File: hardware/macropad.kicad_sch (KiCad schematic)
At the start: 26 parts, among them J2 Conn_01x06, J3 I2C Screen, J4 SPI Screen, SW1 SW_Push, SW2 SW_Push, SW3 SW_Push, SW4 SW_Push, SW5 SW_Push, SW6 SW_Push, SW7 SW_Push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

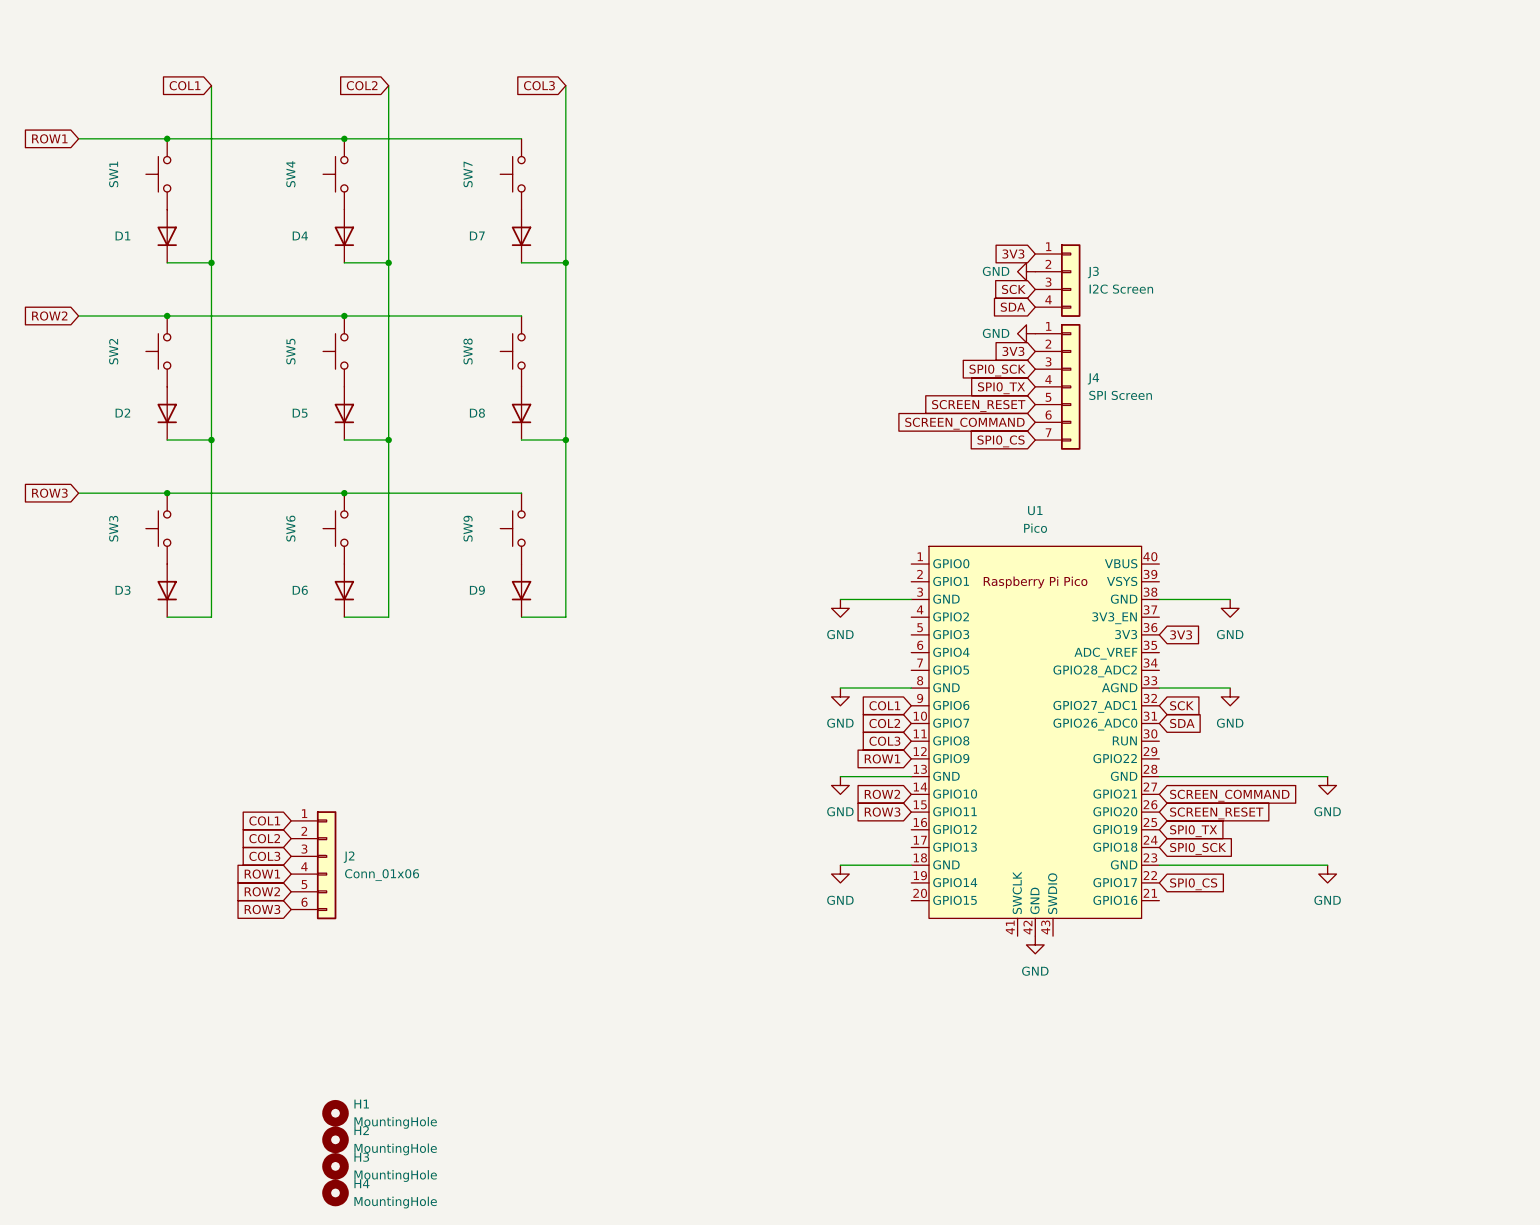
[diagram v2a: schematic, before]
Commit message: :truck: Test different layout with pi pico in the back
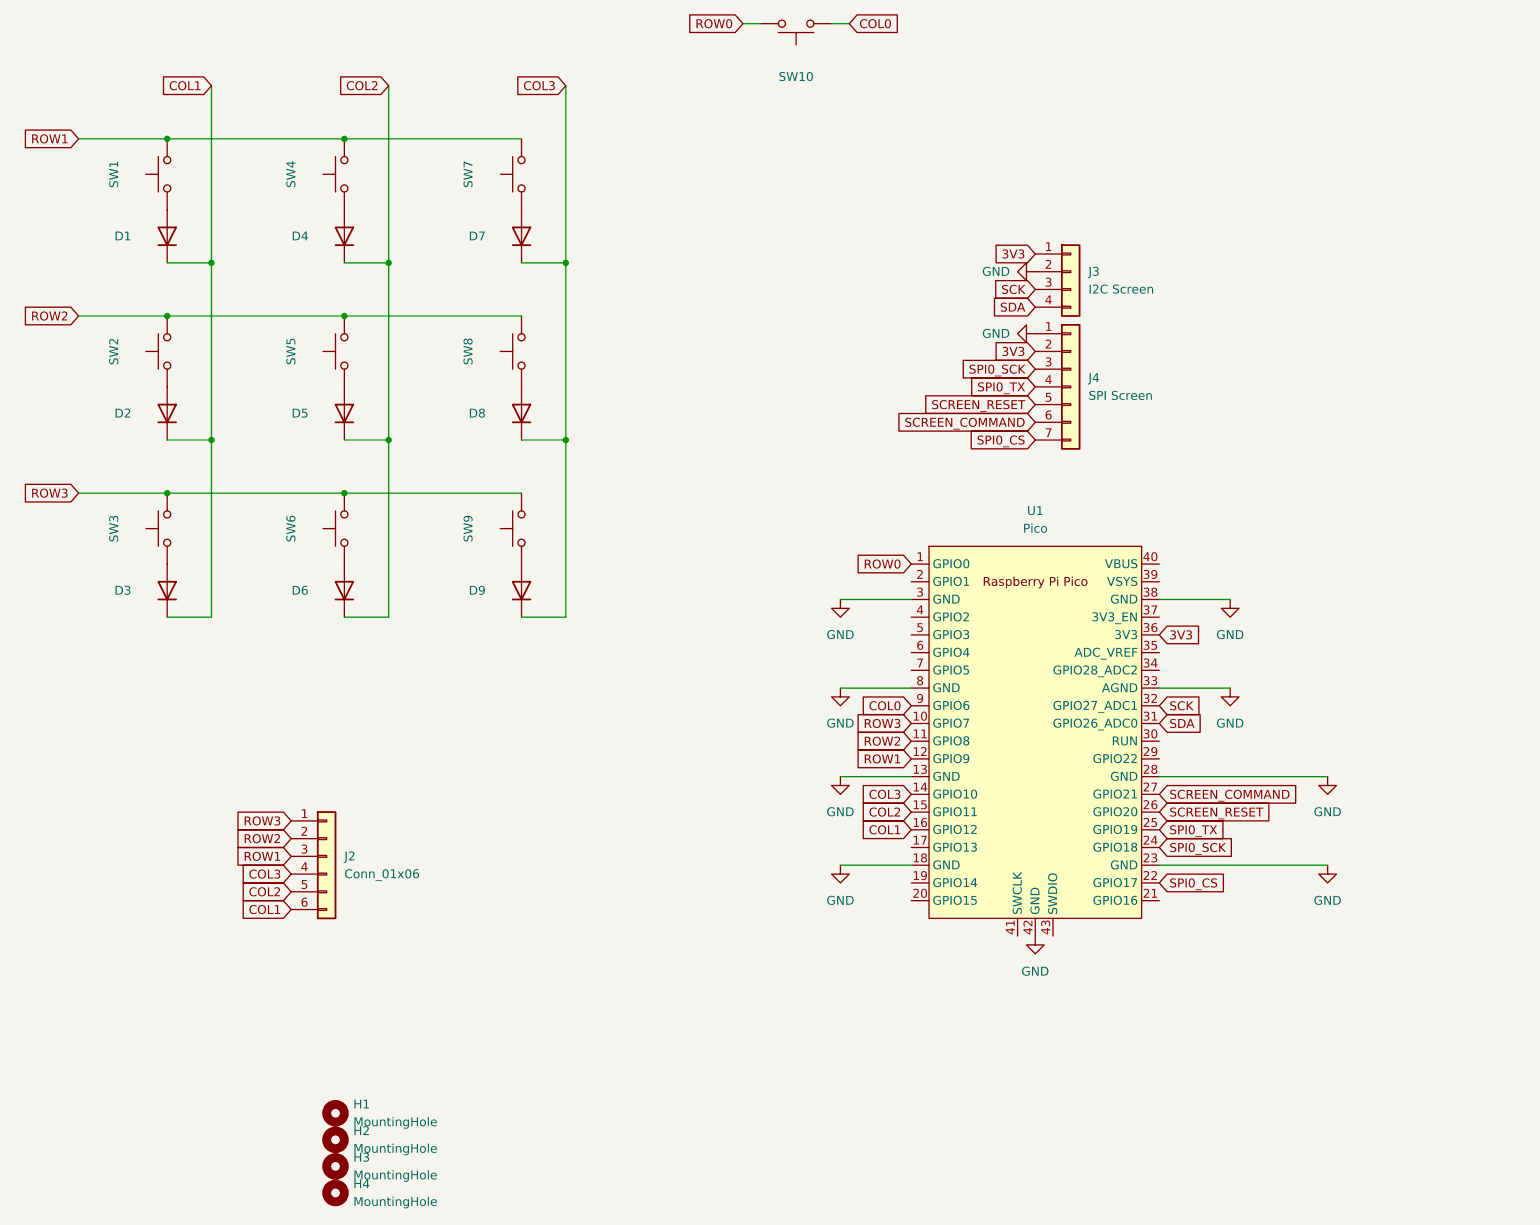
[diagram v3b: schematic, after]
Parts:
- added SW10: SW_Push, Switch_Keyboard_Hotswap_Kailh:SW_Hotswap_Kailh_MX, symbol Switch:SW_Push
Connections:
- net COL1: now also J2.6 (Pin_6), U1.16 (GPIO12); no longer J2.1 (Pin_1), U1.9 (GPIO6)
- net COL2: now also J2.5 (Pin_5), U1.15 (GPIO11); no longer J2.2 (Pin_2), U1.10 (GPIO7)
- net COL3: now also J2.4 (Pin_4), U1.14 (GPIO10); no longer J2.3 (Pin_3), U1.11 (GPIO8)
- net ROW1: now also J2.3 (Pin_3); no longer J2.4 (Pin_4)
- net ROW2: now also J2.2 (Pin_2), U1.11 (GPIO8); no longer J2.5 (Pin_5), U1.14 (GPIO10)
- net ROW3: now also J2.1 (Pin_1), U1.10 (GPIO7); no longer J2.6 (Pin_6), U1.15 (GPIO11)
- net ROW0: now reaches U1.1 (GPIO0)
- net ROW0: now also SW10.1
- new net COL0: SW10.2, U1.9 (GPIO6)
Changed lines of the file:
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@@
+    (stroke (width 0) (type default) (color 0 0 0 0))
+  )
+  (wire (pts (xy 177.8 22.86) (xy 175.26 22.86))
     (stroke (width 0) (type default) (color 0 0 0 0))
   )
@@
   )
   (wire (pts (xy 80.01 90.17) (xy 105.41 90.17))
+    (stroke (width 0) (type default) (color 0 0 0 0))
+  )
+  (wire (pts (xy 162.56 22.86) (xy 165.1 22.86))
     (stroke (width 0) (type default) (color 0 0 0 0))
   )
@@
     )
   )
+  (global_label "ROW0" (shape input) (at 186.69 100.33 180) (fields_autoplaced)
+    (effects (font (size 1.27 1.27)) (justify right))
+    (property "Intersheet References" "${INTERSHEET_REFS}" (id 0) (at 179.0155 100.2506 0)
+      (effects (font (size 1.27 1.27)) (justify right) hide)
+    )
+  )
   (global_label "SCK" (shape input) (at 204.47 60.96 180) (fields_autoplaced)
     (effects (font (size 1.27 1.27)) (justify right))
@@
     )
   )
-  (global_label "COL2" (shape input) (at 97.79 139.7 180) (fields_autoplaced)
-    (effects (font (size 1.27 1.27)) (justify right))
-    (property "Intersheet References" "${INTERSHEET_REFS}" (id 0) (at 90.5388 139.6206 0)
+  (global_label "COL2" (shape input) (at 97.79 147.32 180) (fields_autoplaced)
+    (effects (font (size 1.27 1.27)) (justify right))
+    (property "Intersheet References" "${INTERSHEET_REFS}" (id 0) (at 90.5388 147.3994 0)
       (effects (font (size 1.27 1.27)) (justify right) hide)
     )
@@
     )
   )
-  (global_label "COL3" (shape input) (at 186.69 125.73 180) (fields_autoplaced)
-    (effects (font (size 1.27 1.27)) (justify right))
-    (property "Intersheet References" "${INTERSHEET_REFS}" (id 0) (at 179.4388 125.6506 0)
-      (effects (font (size 1.27 1.27)) (justify right) hide)
-    )
-  )
-  (global_label "ROW3" (shape input) (at 186.69 135.89 180) (fields_autoplaced)
-    (effects (font (size 1.27 1.27)) (justify right))
-    (property "Intersheet References" "${INTERSHEET_REFS}" (id 0) (at 179.0155 135.8106 0)
+  (global_label "COL3" (shape input) (at 186.69 133.35 180) (fields_autoplaced)
+    (effects (font (size 1.27 1.27)) (justify right))
+    (property "Intersheet References" "${INTERSHEET_REFS}" (id 0) (at 179.4388 133.2706 0)
+      (effects (font (size 1.27 1.27)) (justify right) hide)
+    )
+  )
+  (global_label "ROW3" (shape input) (at 186.69 123.19 180) (fields_autoplaced)
+    (effects (font (size 1.27 1.27)) (justify right))
+    (property "Intersheet References" "${INTERSHEET_REFS}" (id 0) (at 179.0155 123.1106 0)
       (effects (font (size 1.27 1.27)) (justify right) hide)
     )
@@
     )
   )
-  (global_label "COL3" (shape input) (at 97.79 142.24 180) (fields_autoplaced)
-    (effects (font (size 1.27 1.27)) (justify right))
-    (property "Intersheet References" "${INTERSHEET_REFS}" (id 0) (at 90.5388 142.1606 0)
-      (effects (font (size 1.27 1.27)) (justify right) hide)
-    )
-  )
-  (global_label "COL1" (shape input) (at 97.79 137.16 180) (fields_autoplaced)
-    (effects (font (size 1.27 1.27)) (justify right))
-    (property "Intersheet References" "${INTERSHEET_REFS}" (id 0) (at 90.5388 137.0806 0)
-      (effects (font (size 1.27 1.27)) (justify right) hide)
-    )
-  )
-  (global_label "COL1" (shape input) (at 186.69 120.65 180) (fields_autoplaced)
-    (effects (font (size 1.27 1.27)) (justify right))
-    (property "Intersheet References" "${INTERSHEET_REFS}" (id 0) (at 179.4388 120.5706 0)
+  (global_label "COL3" (shape input) (at 97.79 144.78 180) (fields_autoplaced)
+    (effects (font (size 1.27 1.27)) (justify right))
+    (property "Intersheet References" "${INTERSHEET_REFS}" (id 0) (at 90.5388 144.8594 0)
+      (effects (font (size 1.27 1.27)) (justify right) hide)
+    )
+  )
+  (global_label "COL1" (shape input) (at 97.79 149.86 180) (fields_autoplaced)
+    (effects (font (size 1.27 1.27)) (justify right))
+    (property "Intersheet References" "${INTERSHEET_REFS}" (id 0) (at 90.5388 149.9394 0)
+      (effects (font (size 1.27 1.27)) (justify right) hide)
+    )
+  )
+  (global_label "COL1" (shape input) (at 186.69 138.43 180) (fields_autoplaced)
+    (effects (font (size 1.27 1.27)) (justify right))
+    (property "Intersheet References" "${INTERSHEET_REFS}" (id 0) (at 179.4388 138.3506 0)
       (effects (font (size 1.27 1.27)) (justify right) hide)
     )
@@
     )
   )
+  (global_label "COL0" (shape input) (at 177.8 22.86 0) (fields_autoplaced)
+    (effects (font (size 1.27 1.27)) (justify left))
+    (property "Intersheet References" "${INTERSHEET_REFS}" (id 0) (at 185.0512 22.9394 0)
+      (effects (font (size 1.27 1.27)) (justify left) hide)
+    )
+  )
   (global_label "SDA" (shape input) (at 222.25 123.19 0) (fields_autoplaced)
     (effects (font (size 1.27 1.27)) (justify left))
@@
     )
   )
-  (global_label "COL2" (shape input) (at 186.69 123.19 180) (fields_autoplaced)
-    (effects (font (size 1.27 1.27)) (justify right))
-    (property "Intersheet References" "${INTERSHEET_REFS}" (id 0) (at 179.4388 123.1106 0)
+  (global_label "COL2" (shape input) (at 186.69 135.89 180) (fields_autoplaced)
+    (effects (font (size 1.27 1.27)) (justify right))
+    (property "Intersheet References" "${INTERSHEET_REFS}" (id 0) (at 179.4388 135.8106 0)
       (effects (font (size 1.27 1.27)) (justify right) hide)
     )
@@
     (effects (font (size 1.27 1.27)) (justify right))
     (property "Intersheet References" "${INTERSHEET_REFS}" (id 0) (at 198.5493 69.9294 0)
+      (effects (font (size 1.27 1.27)) (justify right) hide)
+    )
+  )
+  (global_label "COL0" (shape input) (at 186.69 120.65 180) (fields_autoplaced)
+    (effects (font (size 1.27 1.27)) (justify right))
+    (property "Intersheet References" "${INTERSHEET_REFS}" (id 0) (at 179.4388 120.5706 0)
       (effects (font (size 1.27 1.27)) (justify right) hide)
     )
@@
     )
   )
-  (global_label "ROW2" (shape input) (at 97.79 147.32 180) (fields_autoplaced)
-    (effects (font (size 1.27 1.27)) (justify right))
-    (property "Intersheet References" "${INTERSHEET_REFS}" (id 0) (at 90.1155 147.2406 0)
+  (global_label "ROW2" (shape input) (at 97.79 139.7 180) (fields_autoplaced)
+    (effects (font (size 1.27 1.27)) (justify right))
+    (property "Intersheet References" "${INTERSHEET_REFS}" (id 0) (at 90.1155 139.7794 0)
       (effects (font (size 1.27 1.27)) (justify right) hide)
     )
@@
     )
   )
-  (global_label "ROW1" (shape input) (at 97.79 144.78 180) (fields_autoplaced)
-    (effects (font (size 1.27 1.27)) (justify right))
-    (property "Intersheet References" "${INTERSHEET_REFS}" (id 0) (at 90.1155 144.7006 0)
-      (effects (font (size 1.27 1.27)) (justify right) hide)
-    )
-  )
-  (global_label "ROW3" (shape input) (at 97.79 149.86 180) (fields_autoplaced)
-    (effects (font (size 1.27 1.27)) (justify right))
-    (property "Intersheet References" "${INTERSHEET_REFS}" (id 0) (at 90.1155 149.7806 0)
+  (global_label "ROW1" (shape input) (at 97.79 142.24 180) (fields_autoplaced)
+    (effects (font (size 1.27 1.27)) (justify right))
+    (property "Intersheet References" "${INTERSHEET_REFS}" (id 0) (at 90.1155 142.3194 0)
+      (effects (font (size 1.27 1.27)) (justify right) hide)
+    )
+  )
+  (global_label "ROW3" (shape input) (at 97.79 137.16 180) (fields_autoplaced)
+    (effects (font (size 1.27 1.27)) (justify right))
+    (property "Intersheet References" "${INTERSHEET_REFS}" (id 0) (at 90.1155 137.2394 0)
+      (effects (font (size 1.27 1.27)) (justify right) hide)
+    )
+  )
+  (global_label "ROW0" (shape input) (at 162.56 22.86 180) (fields_autoplaced)
+    (effects (font (size 1.27 1.27)) (justify right))
+    (property "Intersheet References" "${INTERSHEET_REFS}" (id 0) (at 154.8855 22.7806 0)
       (effects (font (size 1.27 1.27)) (justify right) hide)
     )
@@
     )
   )
-  (global_label "ROW2" (shape input) (at 186.69 133.35 180) (fields_autoplaced)
-    (effects (font (size 1.27 1.27)) (justify right))
-    (property "Intersheet References" "${INTERSHEET_REFS}" (id 0) (at 179.0155 133.2706 0)
+  (global_label "ROW2" (shape input) (at 186.69 125.73 180) (fields_autoplaced)
+    (effects (font (size 1.27 1.27)) (justify right))
+    (property "Intersheet References" "${INTERSHEET_REFS}" (id 0) (at 179.0155 125.6506 0)
       (effects (font (size 1.27 1.27)) (justify right) hide)
     )
@@
     )
     (pin "1")
+  )
+  (symbol (lib_id "Switch:SW_Push") (at 170.18 22.86 0) (mirror x) (unit 1)
+    (in_bom yes) (on_board yes)
+    (property "Reference" "SW10" (id 0) (at 170.18 30.48 0))
+    (property "Value" "SW_Push" (id 1) (at 170.18 17.78 90)
+      (effects (font (size 1.27 1.27)) hide)
+    )
+    (property "Footprint" "Switch_Keyboard_Hotswap_Kailh:SW_Hotswap_Kailh_MX" (id 2) (at 170.18 27.94 0)
+      (effects (font (size 1.27 1.27)) hide)
+    )
+    (property "Datasheet" "~" (id 3) (at 170.18 27.94 0)
+      (effects (font (size 1.27 1.27)) hide)
+    )
+    (pin "1")
+    (pin "2")
   )
   (symbol (lib_id "Switch:SW_Push") (at 80.01 95.25 90) (mirror x) (unit 1)
@@
       (reference "SW9") (unit 1) (value "SW_Push") (footprint "Switch_Keyboard_Hotswap_Kailh:SW_Hotswap_Kailh_MX")
     )
+    (path "/bfa19d0e-c090-4ec1-a6e2-d48d96645782"
+      (reference "SW10") (unit 1) (value "SW_Push") (footprint "Switch_Keyboard_Hotswap_Kailh:SW_Hotswap_Kailh_MX")
+    )
     (path "/f8f0ac85-0552-4075-8147-74e9d1f88745"

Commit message: :construction: Some routing
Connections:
- net COL1: now also J2.1 (Pin_1); no longer J2.6 (Pin_6)
- net COL2: now also J2.2 (Pin_2); no longer J2.5 (Pin_5)
- net COL3: now also J2.3 (Pin_3); no longer J2.4 (Pin_4)
- net ROW1: now also J2.4 (Pin_4); no longer J2.3 (Pin_3)
- net ROW2: now also J2.5 (Pin_5); no longer J2.2 (Pin_2)
- net ROW3: now also J2.6 (Pin_6); no longer J2.1 (Pin_1)
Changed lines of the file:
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@@
     (pin "2")
   )
-  (symbol (lib_id "Connector_Generic:Conn_01x06") (at 102.87 142.24 0) (unit 1)
+  (symbol (lib_id "Connector_Generic:Conn_01x06") (at 102.87 144.78 0) (mirror x) (unit 1)
     (in_bom yes) (on_board yes) (fields_autoplaced)
-    (property "Reference" "J2" (id 0) (at 105.41 142.2399 0)
-      (effects (font (size 1.27 1.27)) (justify left))
-    )
-    (property "Value" "Conn_01x06" (id 1) (at 105.41 144.7799 0)
-      (effects (font (size 1.27 1.27)) (justify left))
-    )
-    (property "Footprint" "Connector_PinHeader_2.54mm:PinHeader_1x06_P2.54mm_Vertical" (id 2) (at 102.87 142.24 0)
+    (property "Reference" "J2" (id 0) (at 102.87 130.81 0))
+    (property "Value" "Conn_01x06" (id 1) (at 102.87 133.35 0))
+    (property "Footprint" "Connector_PinHeader_2.54mm:PinHeader_1x06_P2.54mm_Vertical" (id 2) (at 102.87 144.78 0)
       (effects (font (size 1.27 1.27)) hide)
     )
-    (property "Datasheet" "~" (id 3) (at 102.87 142.24 0)
+    (property "Datasheet" "~" (id 3) (at 102.87 144.78 0)
       (effects (font (size 1.27 1.27)) hide)
     )
